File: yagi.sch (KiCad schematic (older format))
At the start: 57 parts, among them IC1 AT24CS32-SSHM, J1 RPi_GPIO, P1 HV+, P10 CONN_01X02, P11 CONN_01X02, P12 CONN_01X03, P2 HV-, P3 CONN_01X01, P4 CONN_01X01, P5 CONN_01X02, P6 CONN_01X03, P7 CONN_01X02, P8 CONN_01X03, P9 CONN_01X03, Q1 STN0214, Q2 STN0214, Q3 MMBT4401, U1 74LS244

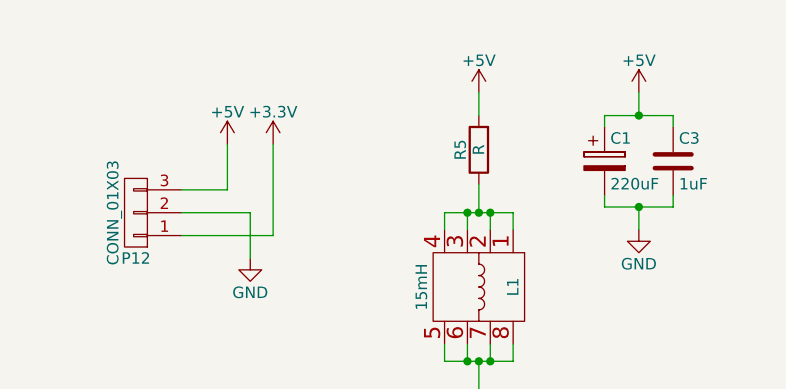
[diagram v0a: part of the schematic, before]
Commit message: Add pins for easy current measurement for coil.
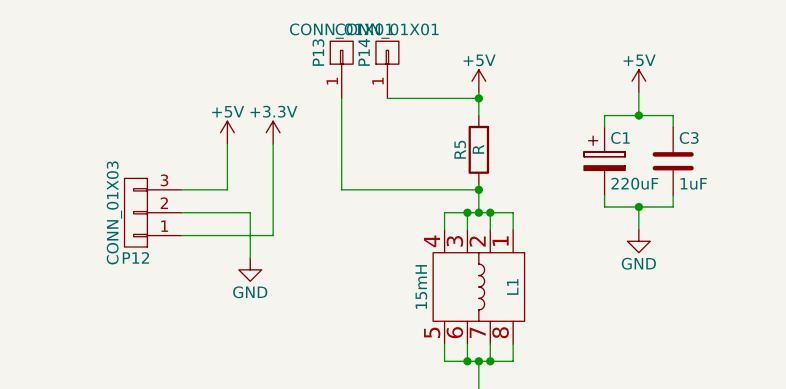
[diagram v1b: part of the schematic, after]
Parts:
- added P13, P14: CONN_01X01, Wire_Pads:SolderWirePad_single_0-8mmDrill, symbol CONN_01X01
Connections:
- net +5V: now also P14.1 (P1)
- net at L1.1, L1.2, L1.3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: now also P13.1 (P1)
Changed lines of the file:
@@
 Wire Wire Line
 	1500 1500 1500 1100
+$Comp
+L CONN_01X01 P14
+U 1 1 560FC371
+P 2000 700
+F 0 "P14" H 2000 800 50  0000 C CNN
+F 1 "CONN_01X01" V 2100 700 50  0000 C CNN
+F 2 "Wire_Pads:SolderWirePad_single_0-8mmDrill" H 2000 700 60  0001 C CNN
+F 3 "" H 2000 700 60  0000 C CNN
+	1    2000 700
+	0    -1   -1   0
+$EndComp
+$Comp
+L CONN_01X01 P13
+U 1 1 560FC464
+P 1800 700
+F 0 "P13" H 1800 800 50  0000 C CNN
+F 1 "CONN_01X01" V 1900 700 50  0000 C CNN
+F 2 "Wire_Pads:SolderWirePad_single_0-8mmDrill" H 1800 700 60  0001 C CNN
+F 3 "" H 1800 700 60  0000 C CNN
+	1    1800 700
+	0    -1   -1   0
+$EndComp
+Wire Wire Line
+	2000 900  2400 900
+Connection ~ 2400 900
+Wire Wire Line
+	1800 900  1800 1300
+Wire Wire Line
+	1800 1300 2400 1300
+Connection ~ 2400 1300
 $EndSCHEMATC

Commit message: New try.
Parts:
- removed C2, C4: 47nF, Capacitors_SMD:C_0805, symbol C
- removed D3: RFU02VSM8STR, chenit:TUMD2SM, symbol D
- removed P1: HV+, Wire_Pads:SolderWirePad_single_1-2mmDrill, symbol CONN_01X01
- removed P13, P14: CONN_01X01, Wire_Pads:SolderWirePad_single_0-8mmDrill, symbol CONN_01X01
- removed Q1: STN0214, chenit:SOT223, symbol Q_NPN_BCEC
- removed R7: R, Resistors_SMD:R_0805_HandSoldering, symbol R
- added C1: 1nF, Capacitors_SMD:C_0805_HandSoldering, symbol C
- added C11, C12: 0.1uF, Capacitors_SMD:C_0603_HandSoldering, symbol C
- added C2, C3: 47nF, Capacitors_SMD:C_1210_HandSoldering, symbol C_Small
- added D1: 1N4148, Discret:DO-35, symbol D
- added D2: D, chenit:TUMD2SM, symbol D
- added P10, P4: CONN_01X02, Pin_Headers:Pin_Header_Straight_1x02, symbol CONN_01X02
- added P13: CONN_01X03, Pin_Headers:Pin_Header_Straight_1x03, symbol CONN_01X03
- added P2, P3: CONN_01X01, chenit:PIN, symbol CONN_01X01
- added P5: HV+, Wire_Pads:SolderWirePad_single_1-2mmDrill, symbol CONN_01X01
- added Q1: MMBT4401, TO_SOT_Packages_SMD:SOT-23, symbol Q_NPN_BEC
- added Q3: STN0214, TO_SOT_Packages_SMD:SOT-223, symbol Q_NPN_BCEC
- added R1, R12, R4: R, Resistors_SMD:R_0805_HandSoldering, symbol R
- added R2: 220k, Resistors_SMD:R_0805_HandSoldering, symbol R
- added R3: RV-TG, chenit:bourns-3361-p, symbol RV-TG
- added U1: TLC555, Housings_SOIC:SOIC-8_3.9x4.9mm_Pitch1.27mm, symbol TLC555
- C10: renamed from C6; footprint Capacitors_SMD:C_0805 -> Capacitors_SMD:C_0603_HandSoldering
- C4: renamed from C5; footprint Capacitors_SMD:C_0603 -> Capacitors_SMD:C_0603_HandSoldering
- C7: renamed from C3; footprint Capacitors_SMD:C_0603 -> Capacitors_SMD:C_0805_HandSoldering
- C8: footprint Capacitors_SMD:C_0805 -> Capacitors_SMD:C_0805_HandSoldering
- C9: footprint Capacitors_SMD:C_0805 -> Capacitors_SMD:C_0603_HandSoldering
- L1: value 15mH -> SRR0908-Y
- Q2: footprint chenit:SOT223 -> TO_SOT_Packages_SMD:SOT-223
- R17: renamed from R9; value R -> 1.5k
- R18: renamed from R10; value R -> 100k
- R19: renamed from R11; value R -> 27k
- R6: value R -> 330R
- R8: value 10M -> R
- U2: renamed from U1; footprint Housings_SOIC:SOIC-20_7.5x12.8mm_Pitch1.27mm -> Housings_SSOP:TSSOP-20_4.4x6.5mm_Pitch0.65mm
- renumbered C1 to C5, C7 to C6, D4 to D3, D5 to D4, D6 to D5, D7 to D6, D1 to D7, D2 to D8, P6 to P1, P12 to P11, P8 to P12, P9 to P14, P5 to P15, P10 to P16, P11 to P17, P7 to P6, P2 to P7, P3 to P8, P4 to P9, Q3 to Q4, R17 to R10, R18 to R11, R19 to R13, R20 to R14, R21 to R15, R22 to R16, R1 to R20, R2 to R21, R3 to R22, R4 to R23, R12 to R24, R13 to R25, R14 to R26, R15 to R7, R16 to R9
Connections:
- net +3V3: now also C11.1
- net +5V: now also L1.1, L1.2, L1.3, L1.4, C12.1, R1.1, U1.8 (VCC); no longer R5.2
- net DISC: now also Q3.1 (B)
- net GND: now also C1.2, C11.2, C12.2, C2.2, C3.2, Q1.2 (E), Q3.3 (E), R2.2, R3.1, R3.2, R4.2, U1.1 (GND), U1.6 (THR); no longer Q2.3 (E)
- net at R6.2: now also D1.2 (A), U1.3 (Q)
- net at L1.5, L1.6, L1.7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: now also Q2.2 (C), Q2.4 (C), D2.2 (A)
- net at R8.1: now also C3.1, R12.1
- net at R8.2: now also R5.1, Q3.2 (C), Q3.4 (C)
- net at R23.1: no longer Q2.1 (B)
- net at J1.11 (GPIO17): now also P13.3 (P3)
- net at J1.13 (GPIO27): now also P13.2 (P2)
- net at J1.15 (GPIO22): now also P13.1 (P1)
- new net: Q1.1 (B), Q2.3 (E), R3.3, R4.1
- new net: C2.1, D2.1 (K), R5.2
- new net: P5.1 (P1), R12.2
- new net: R2.1, U1.2 (TR)
- new net: P4.1 (P1), R6.1, U1.7 (DIS)
- new net: C1.1, D1.1 (K)
- new net RST: P2.1 (P1), Q1.3 (C), R1.2, U1.4 (R)
- new net TRG: P10.2 (P2), P3.1 (P1), P4.2 (P2), Q2.1 (B)
- no-connect marks 0 -> 1
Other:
- moved on the sheet: C10, C4, C5, C6, C7, C8, D3, D4, D5, D6, D7, D8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
